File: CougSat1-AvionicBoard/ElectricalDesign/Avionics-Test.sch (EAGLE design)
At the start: 213 parts, among them J1 +X Panel GPS, J10 iFJR SD1, J11 -Y, J12 +Z, J13 +X, J14 -Z, J15 +Y, J16 IFJR SD0, J2 IHU SD1, J3 SWD, J4 CougSat Card, J5 -X, J6 IHU SD0, J8 SWD, J9 SWD, U1 STM32L476RGT, U10 BNO055, U11 M24M01, U12 TXS0102DQM, U13 TXS0102DQM, U14 AD8515, U15 BNO055, U16 BNO055, U17 TXS0102DQM, U18 TXS0102DQM, U19 AD8515, U2 STM32L476RGT, U20 INA199C2, U21 INA199C2, U22 TXS0102DQM, U23 TXS0102DQM, U24 AD8515, U25 AD7291, U26 AD7291, U27 TXS0102DQM, U28 INA199C2, U29 AD8515, U3 STM32L476RGT, U30 DRV8837, U4 M24M01, U5 TXS0102DQM, U6 DRV8837, U7 DRV8837, U8 AD7291, U9 Venus838FLPx-L, Y1 8MHz ±10ppm, Y10 32.768kHz ±10ppm, Y2 32.768kHz ±10ppm, Y3 8MHz ±10ppm, Y4 32.768kHz ±10ppm, Y5 8MHz ±10ppm, Y6 32.768kHz ±10ppm, Y7 32.768kHz ±10ppm, Y8 32.768kHz ±10ppm

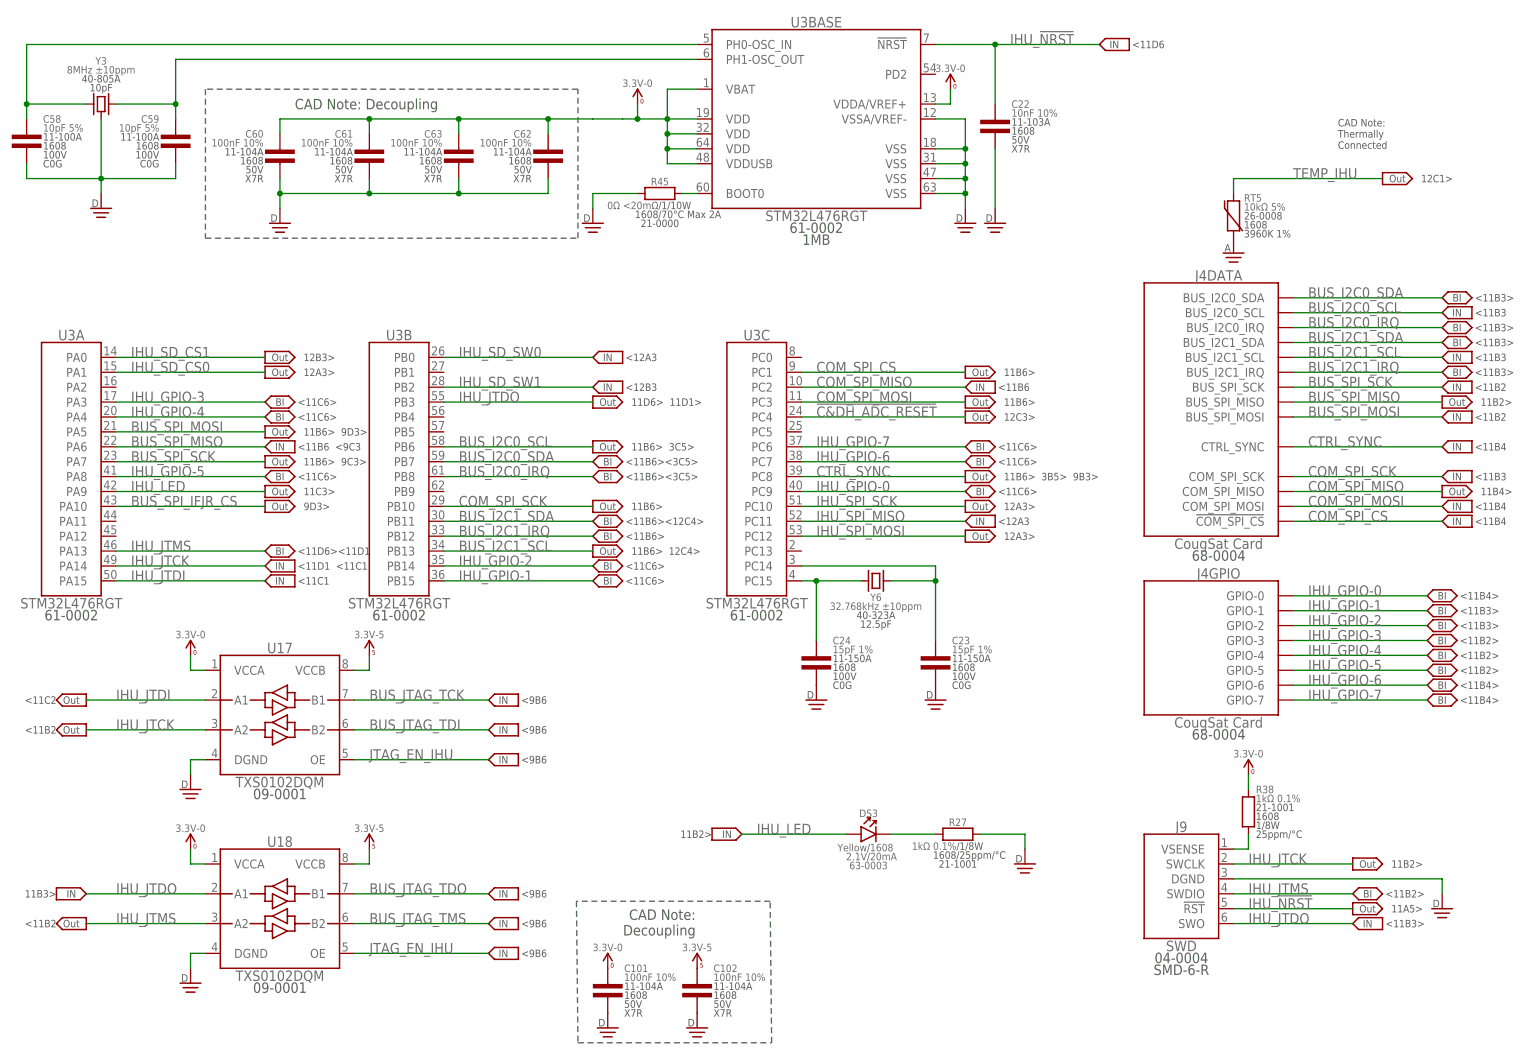
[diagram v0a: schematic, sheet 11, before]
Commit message: Rearranged IHU GPIO for Routing
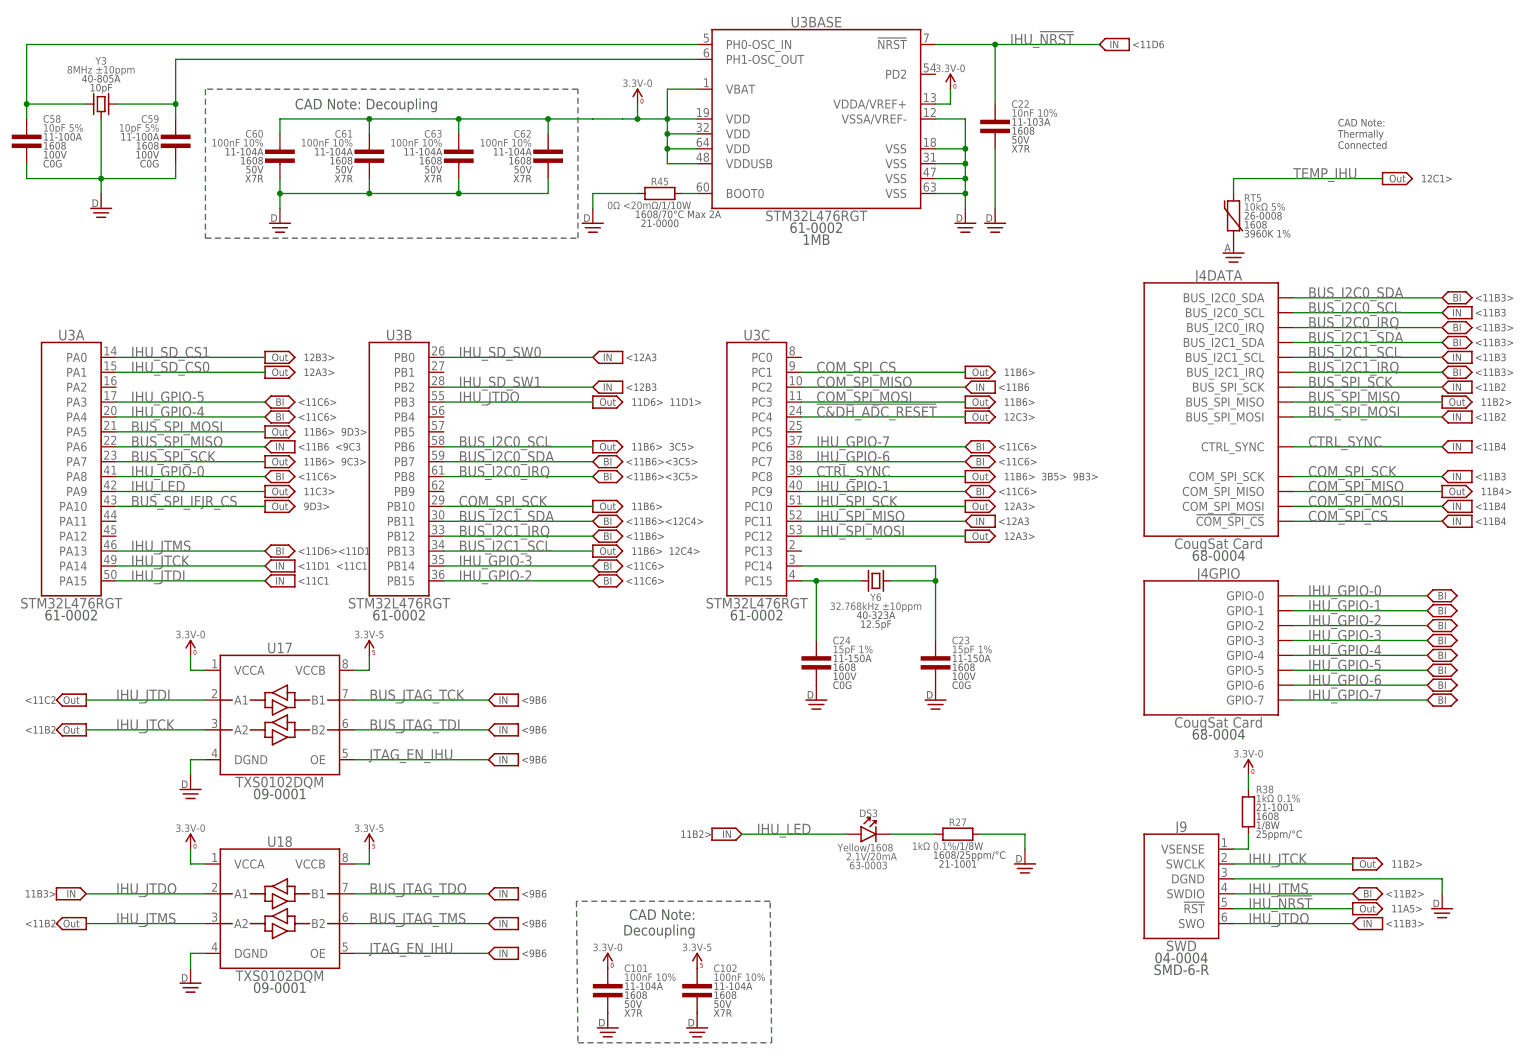
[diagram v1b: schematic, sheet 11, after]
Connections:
- net IHU_GPIO-0: now also U3A.PA8; no longer U3C.PC9
- net IHU_GPIO-1: now also U3C.PC9; no longer U3B.PB15
- net IHU_GPIO-2: now also U3B.PB15; no longer U3B.PB14
- net IHU_GPIO-3: now also U3B.PB14; no longer U3A.PA3
- net IHU_GPIO-5: now also U3A.PA3; no longer U3A.PA8
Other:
- note removed: "<11B4>"

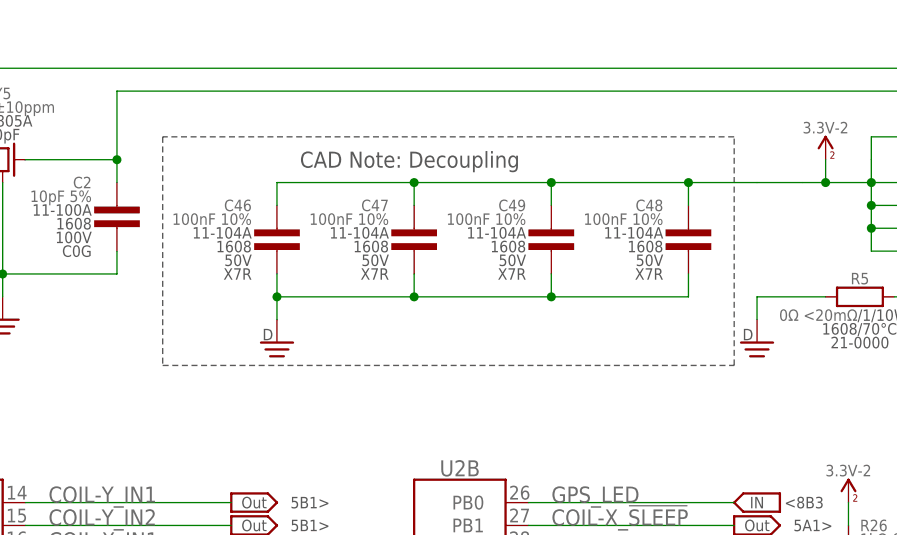
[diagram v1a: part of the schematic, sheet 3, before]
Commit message: Routed 4 Layer Avionics Board
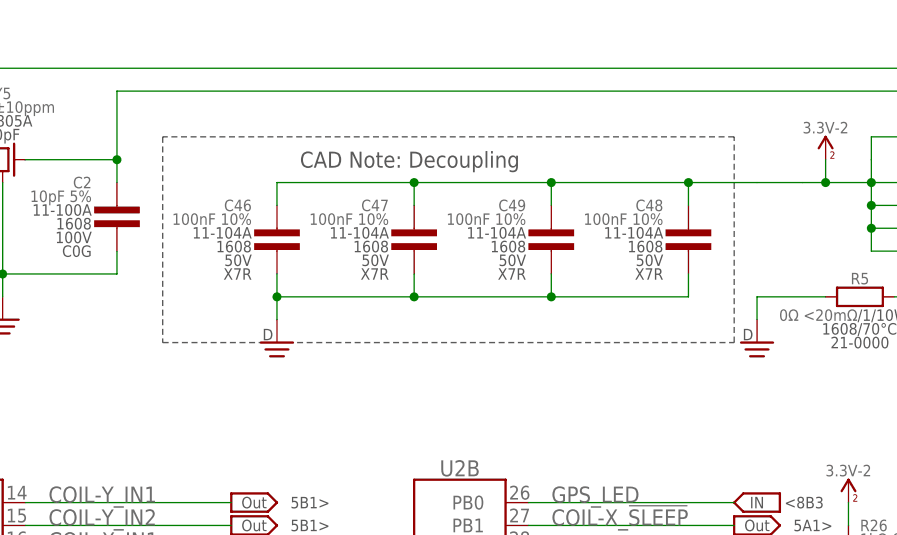
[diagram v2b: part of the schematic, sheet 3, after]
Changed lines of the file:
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@@
 <?xml version="1.0" encoding="utf-8"?>
 <!DOCTYPE eagle SYSTEM "eagle.dtd">
-<eagle version="9.5.2">
+<eagle version="9.6.2">
 <drawing>
 <settings>
@@
 <text x="48.26" y="124.46" size="1.27" layer="97" align="center-left">   3D5&gt;</text>
 <text x="200.66" y="40.64" size="1.27" layer="97" align="center-right">3B2&gt; </text>
-<wire x1="35.56" y1="177.8" x2="35.56" y2="152.4" width="0.1524" layer="97" style="shortdash"/>
-<wire x1="35.56" y1="152.4" x2="99.06" y2="152.4" width="0.1524" layer="97" style="shortdash"/>
-<wire x1="99.06" y1="152.4" x2="99.06" y2="177.8" width="0.1524" layer="97" style="shortdash"/>
+<wire x1="35.56" y1="177.8" x2="35.56" y2="154.94" width="0.1524" layer="97" style="shortdash"/>
+<wire x1="35.56" y1="154.94" x2="99.06" y2="154.94" width="0.1524" layer="97" style="shortdash"/>
+<wire x1="99.06" y1="154.94" x2="99.06" y2="177.8" width="0.1524" layer="97" style="shortdash"/>
 <wire x1="99.06" y1="177.8" x2="35.56" y2="177.8" width="0.1524" layer="97" style="shortdash"/>
 <text x="50.8" y="175.26" size="1.778" layer="97" align="center-left">CAD Note: Decoupling</text>
